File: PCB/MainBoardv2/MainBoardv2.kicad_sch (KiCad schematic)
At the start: 22 parts, among them J1 Conn_02x03_Odd_Even, SW1 SW_Push, U1 STM32F103C8T6TR

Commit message: Updating progress on board v2
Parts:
- added C11, C12: 20p, Capacitor_SMD:C_0603_1608Metric, symbol basic:C
- added C13: 10u, Capacitor_SMD:C_0603_1608Metric, symbol basic:C
- added C14: 22u, Capacitor_SMD:C_0805_2012Metric, symbol basic:C
- added J2: USB_B_Micro, symbol Connector:USB_B_Micro
- added J3: Conn_01x04_Pin, symbol Connector:Conn_01x04_Pin
- added J4, J7: Screw_Terminal_01x02, local:CONN_1985195, symbol Connector:Screw_Terminal_01x02
- added J5: Conn_02x03_Odd_Even, Connector_PinSocket_2.54mm:PinSocket_2x03_P2.54mm_Vertical, symbol Connector_Generic:Conn_02x03_Odd_Even
- added R4: 1k5, Resistor_SMD:R_0603_1608Metric, symbol basic:R
- added SW2: SW_SP3T, symbol Switch:SW_SP3T
- added U4: AZ1117-3.3, Package_TO_SOT_SMD:TO-252-2, symbol Regulator_Linear:AZ1117-3.3
- added Y1: 8MHz Crystal, Crystal:Crystal_HC49-U_Vertical, symbol Device:Crystal
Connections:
- net +3.3V: now also J3.1 (Pin_1), R4.1
- net GND: now also C11.1, C12.1, C13.2, C14.2, J2.5 (GND), J3.4 (Pin_4), J4.1 (Pin_1), J7.1 (Pin_1), U4.1 (GND)
- net TIM2_CH1: now reaches U1.10 (PA0)
- net TIM2_CH2: now reaches U1.11 (PA1)
- net SPI1_NSS_RasPi: now reaches U1.12 (PA2)
- net SPI1_NSS_ESP2: now reaches U1.13 (PA3)
- net SPI1_NSS_ESP1: now reaches U1.14 (PA4)
- net SPI1_SCK: now reaches U1.15 (PA5)
- net SPI1_MISO: now reaches U1.16 (PA6)
- net SPI1_MOSI: now reaches U1.17 (PA7)
- net TIM1_CH1: now reaches U1.29 (PA8)
- net TIM1_CH2: now reaches U1.30 (PA9)
- net TIM1_CH3: now reaches U1.31 (PA10)
- net USB_D-: now reaches U1.32 (PA11)
- net USB_D-: now also J2.2 (D-)
- net USB_D+: now reaches U1.33 (PA12)
- net USB_D+: now also J2.3 (D+), R4.2
- net SWDIO: now reaches U1.34 (PA13)
- net SWDIO: now also J3.2 (Pin_2)
- net SWCLK: now reaches U1.37 (PA14)
- net SWCLK: now also J3.3 (Pin_3)
- net TIM3_CH1: now reaches U1.40 (PB4)
- net TIM3_CH2: now reaches U1.41 (PB5)
- net TIM4_CH1: now reaches U1.42 (PB6)
- net TIM4_CH2: now reaches U1.43 (PB7)
- net OR3: now reaches U1.46 (PB9)
- net OSC_IN: now reaches U1.5 (PD0)
- net OSC_IN: now also C12.2, Y1.1
- net OSC_OUT: now reaches U1.6 (PD1)
- net OSC_OUT: now also C11.2, Y1.2
- new net +3V3: C14.1, J5.2 (Pin_2), J5.4 (Pin_4), U4.2 (VO)
- new net 12V_EXT: J4.2 (Pin_2)
- new net 5V_BUCK: SW2.2
- new net 5V_EXT: J5.5 (Pin_5), J7.2 (Pin_2), SW2.1
- new net REG_IN: C13.1, J5.3 (Pin_3), SW2.3, U4.3 (VI)
- new net VBUS: J2.1 (VBUS), J5.1 (Pin_1), SW2.4
- no-connect marks 22 -> 15
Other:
- added sheet LimitSwitchORGates (LimitSwitchOR.kicad_sch)
- note added: "+3.3V Power Mux"
- note added: "BOOT PINS"
- note added: "External Power Connectors"
- note added: "HIGH SPEED EXTERNAL (HSE) CRYSTAL OSCILLATOR - 8MHz"
- note added: "Limit Switch OR3"
- note added: "Linear Regulator"
- note added: "Microcontroller"
- note added: "RESET SWITCH"
- note added: "SERIAL WIRE DEBUG CONNECTOR"
- note added: "decide how we want handle this?"
- company: (none) -> University of Illinois Urbana-Champaign
- title: (none) -> ECE445_MainBoard
- moved on the sheet: C1, C10, C2, C3, C4, C5, C6, C7, C8, C9, FB1, J1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

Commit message: Update MainBoardv2.kicad_sch
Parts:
- removed J5: Conn_02x03_Odd_Even, Connector_PinSocket_2.54mm:PinSocket_2x03_P2.54mm_Vertical, symbol Connector_Generic:Conn_02x03_Odd_Even
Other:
- note added: "+3.3V Power Switch & Linear Regulator"
- note removed: "+3.3V Power Mux"
- note removed: "Linear Regulator"
- note removed: "decide how we want handle this?"
- moved on the sheet: C13, C14, SW2, U4

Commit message: updating main board v2 progress
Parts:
- removed C9: 4.7u, Capacitor_SMD:C_0603_1608Metric, symbol basic:C
- added C9: 100n, Capacitor_SMD:C_0603_1608Metric, symbol Device:C
- added Cboot, Cinx: 100nF, Capacitor_SMD:C_0805_2012Metric, symbol Device:C
- added Cff: 100pF, symbol Device:C
- added Cin: 15uF, Capacitor_SMD:C_0805_2012Metric, symbol Device:C
- added Cout: 47uF, Capacitor_SMD:C_1210_3225Metric, symbol Device:C
- added D1, D2, D4: LED, LED_THT:LED_D3.0mm_Clear, symbol Device:LED
- added J17, J18, J19: Conn_01x04_Socket, Connector_PinHeader_2.54mm:PinHeader_1x04_P2.54mm_Vertical, symbol Connector:Conn_01x04_Socket
- added J5: Conn_01x03_Socket, Connector_PinHeader_2.54mm:PinHeader_1x03_P2.54mm_Vertical, symbol Connector:Conn_01x03_Socket
- added L1: 3.3uH, CustomFootprints:IHLP3232DZER3R3M01, symbol Device:L
- added R5, R6, R7: 1.5k, Resistor_SMD:R_0603_1608Metric, symbol basic:R
- added Rfbb: 10k, Resistor_SMD:R_0805_2012Metric, symbol basic:R
- added Rfbt: 73.2k, Resistor_SMD:R_0805_2012Metric, symbol basic:R
- added Rff: 20k, Resistor_SMD:R_0603_1608Metric, symbol basic:R
- added Rpg: 100k, Resistor_SMD:R_0805_2012Metric, symbol basic:R
- added U5: TPS56637RPA, CustomFootprints:RPA0010A, symbol CustomSymbols:TPS56637RPA
- added U6: SN74HCS4075PWR, CustomFootprints:SN74HCS4075PWR, symbol CustomSymbols:SN74HCS4075PWR
- C8: value 100n -> 10u
- R4: value 1k5 -> 1.5k
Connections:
- net +3.3V: now also R5.1
- net 5V_BUCK: now also Cout.1, L1.2, Rfbt.2, Rff.2, Rpg.2
- net GND: now also C9.2, Cin.2, Cinx.2, Cout.2, D1.1 (K), D2.1 (K), D4.1 (K), Rfbb.1, U5.10 (MODE), U5.3 (AGND), U5.9 (PGND), U6.7 (GND)
- net OR3: now also U6.6 (1Y)
- net REG_IN: now also C9.1, R6.1, U6.1 (2A), U6.11 (3A), U6.12 (3B), U6.13 (3C), U6.14 (VCC), U6.2 (2B), U6.8 (2C)
- net SPI1_MISO: now also J17.2 (Pin_2), J18.2 (Pin_2), J19.2 (Pin_2)
- net SPI1_MOSI: now also J17.1 (Pin_1), J18.1 (Pin_1), J19.1 (Pin_1)
- net SPI1_NSS_ESP1: now also J17.4 (Pin_4)
- net SPI1_NSS_ESP2: now also J18.4 (Pin_4)
- net SPI1_NSS_RasPi: now also J19.4 (Pin_4)
- net SPI1_SCK: now also J17.3 (Pin_3), J18.3 (Pin_3), J19.3 (Pin_3)
- net 12V_EXT renamed +12V
- net +12V: now also Cin.1, Cinx.1, R7.1, U5.8 (VIN)
- new net: D1.2 (A), R5.2
- new net: Cff.1, Rff.1
- new net: D4.2 (A), R7.2
- new net: D2.2 (A), R6.2
- new net BOOT: Cboot.1, U5.7 (BOOT)
- new net FB: Cff.2, Rfbb.2, Rfbt.1, U5.2 (FB)
- new net LimitSwitch1: J5.1 (Pin_1), U6.5 (1C)
- new net LimitSwitch2: J5.2 (Pin_2), U6.4 (1B)
- new net LimitSwitch3: J5.3 (Pin_3), U6.3 (1A)
- new net PG: Rpg.1, U5.4 (PG)
- new net SW: Cboot.2, L1.1, U5.6 (SW)
- no-connect marks 15 -> 19
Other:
- removed sheet LimitSwitchORGates
- added sheet PWM & Encoders (PWM.kicad_sch)
- note added: "1x 100nF per VDD pin"
- note added: "4.5V to 28V, 6A Synchronous Buck Converter with ULQ-Mode Efficiency: 92.9% Frequency: 559.31kHz"
- note added: "6A Synchronous Buck Converter"
- note added: "Bypass cap. should be placed close to device"
- note added: "ESP32 (x2) & Raspberry Pi"
- note added: "LEDs"
- note added: "Microcontroller (and USB)"
- note added: "Pin-out using STM32CubeIDE"
- note added: "SPI BUS"
- note added: "USB Application Note: AN4879"
- note added: "Unused inputs should be tied to VCC"
- note added: "VBUS from USB Connector (nom. +5V) Min. 22uF inp./outp. caps"
- note added: "VDDA Filtering"
- note removed: "MOUNTING HOLES"
- note removed: "Microcontroller"
- moved on the sheet: C1, C11, C12, C2, C3, C4, C6, C8, H1, H2, H3, H4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

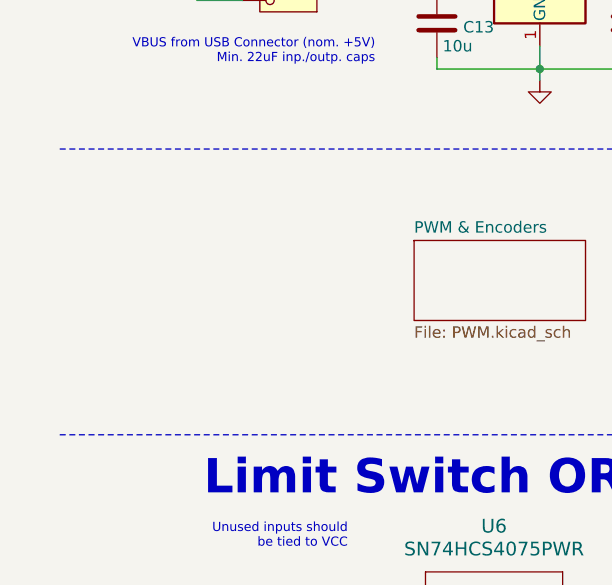
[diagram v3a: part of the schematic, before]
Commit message: updating main board v2 with motor power conns
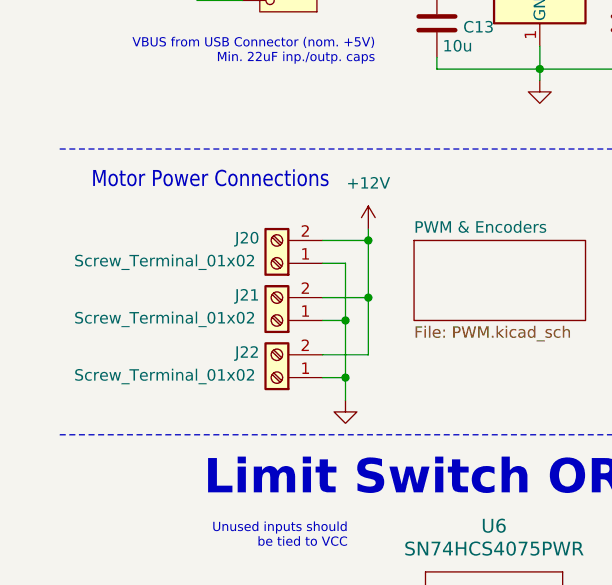
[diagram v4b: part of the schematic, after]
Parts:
- added J20, J21, J22: Screw_Terminal_01x02, local:CONN_1985195, symbol Connector:Screw_Terminal_01x02
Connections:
- net +12V: now also J20.2 (Pin_2), J21.2 (Pin_2), J22.2 (Pin_2)
- net GND: now also J20.1 (Pin_1), J21.1 (Pin_1), J22.1 (Pin_1)
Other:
- note added: "Motor Power Connections"

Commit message: updating progress for board v2
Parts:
- removed J20, J21, J22: Screw_Terminal_01x02, local:CONN_1985195, symbol Connector:Screw_Terminal_01x02
- removed J3: Conn_01x04_Pin, symbol Connector:Conn_01x04_Pin
- added J23: Conn_01x05_Pin, symbol Connector:Conn_01x05_Pin
- added SW4: ~, CustomFootprints:MTM8206NRA, symbol CustomSymbols:SW_Toggle_DPDT
- added TP10, TP7, TP8, TP9: ~, TestPoint:TestPoint_Keystone_5000-5004_Miniature, symbol Connector:TestPoint
- added TP2: 5V, TestPoint:TestPoint_Keystone_5000-5004_Miniature, symbol Connector:TestPoint
- added TP3: 12V, TestPoint:TestPoint_Keystone_5000-5004_Miniature, symbol Connector:TestPoint
- Cff: footprint (none) -> Capacitor_SMD:C_0805_2012Metric
- FB1: footprint (none) -> Inductor_SMD:L_0603_1608Metric
- Rff: footprint Resistor_SMD:R_0603_1608Metric -> Resistor_SMD:R_0805_2012Metric
- TP1: value 3V3 -> 3.3V
- renumbered C5 to C1, C14 to C10, C1 to C11, C11 to C12, C9 to C13, C12 to C14, C7 to C2, C10 to C3, C2 to C4, C3 to C5, C4 to C6, C6 to C7, C13 to C9, Cout to Cout1, D4 to D3, J19 to J10, J17 to J11, J18 to J12, J1 to J4, J5 to J7, J4 to J8, J7 to J9, R5 to R1, R6 to R2, R7 to R3, R1 to R5, R2 to R6, R3 to R7, SW2 to SW1, SW1 to SW2, U4 to U1, U1 to U2, U6 to U3, U5 to U4
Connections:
- net +3V3 is gone; now on net +3.3V: C10.1, U1.2 (VO)
- net +12V: now also D3.2 (A), SW4.2 (B), SW4.5 (B), TP3.1; no longer J8.2 (Pin_2), R3.1
- net +3.3V: now also D1.2 (A), J23.1 (Pin_1); no longer R1.1
- net GND: now also R1.2, R2.2, R3.2, J23.5 (Pin_5); no longer D1.1 (K), D2.1 (K), D3.1 (K)
- net NRST: now also J23.4 (Pin_4)
- net OR3: now also TP7.1
- net REG_IN: now also D2.2 (A), TP2.1; no longer R2.1
- net SPI1_MISO: now also TP9.1
- net SPI1_MOSI: now also TP10.1
- net SPI1_SCK: now also TP8.1
- net SWCLK: now also J23.3 (Pin_3)
- net SWDIO: now also J23.2 (Pin_2)
- net Cff_Rff: now reaches Cff.1, Rff.1
- new net: J8.2 (Pin_2), SW4.1 (A), SW4.4 (A)
- new net PWR_LED_12V_Cathode: D3.1 (K), R3.1
- new net PWR_LED_3V3_Cathode: D1.1 (K), R1.1
- new net PWR_LED_5V_Cathode: D2.1 (K), R2.1
- no-connect marks 19 -> 21
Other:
- added sheet Motors (Motors.kicad_sch)
- note added: "6A Buck chosen to leave headroom for a future iteration where 5V external devices are powered through this board"
- note removed: "Motor Power Connections"
- moved on the sheet: C11, C12, C14, D1, D2, D3, J10, J11, J12, J8, J9, R1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

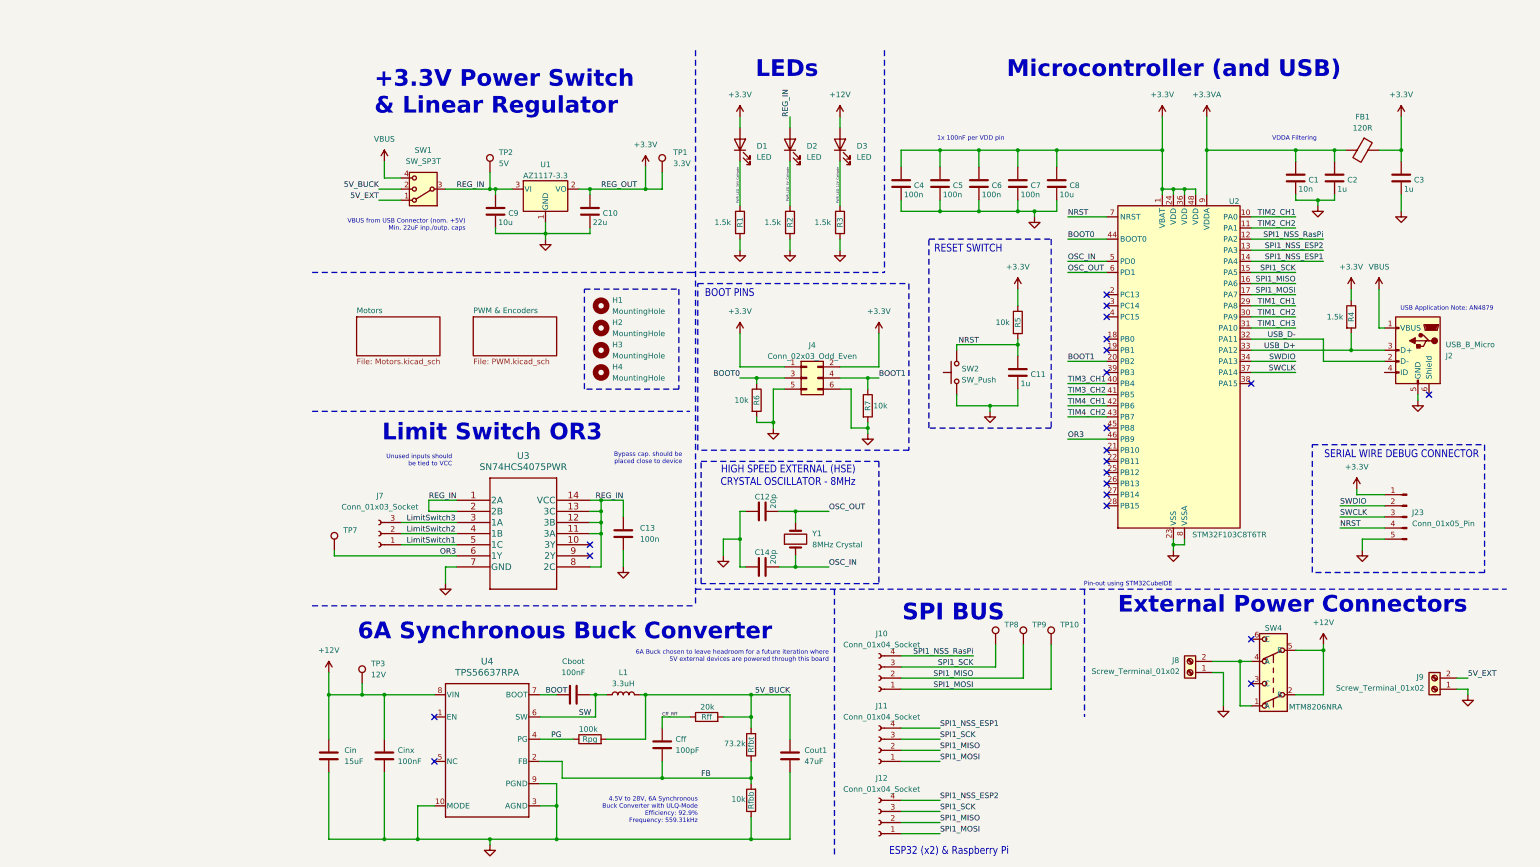
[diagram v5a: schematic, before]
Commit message: board v2 passing ERC in schematic
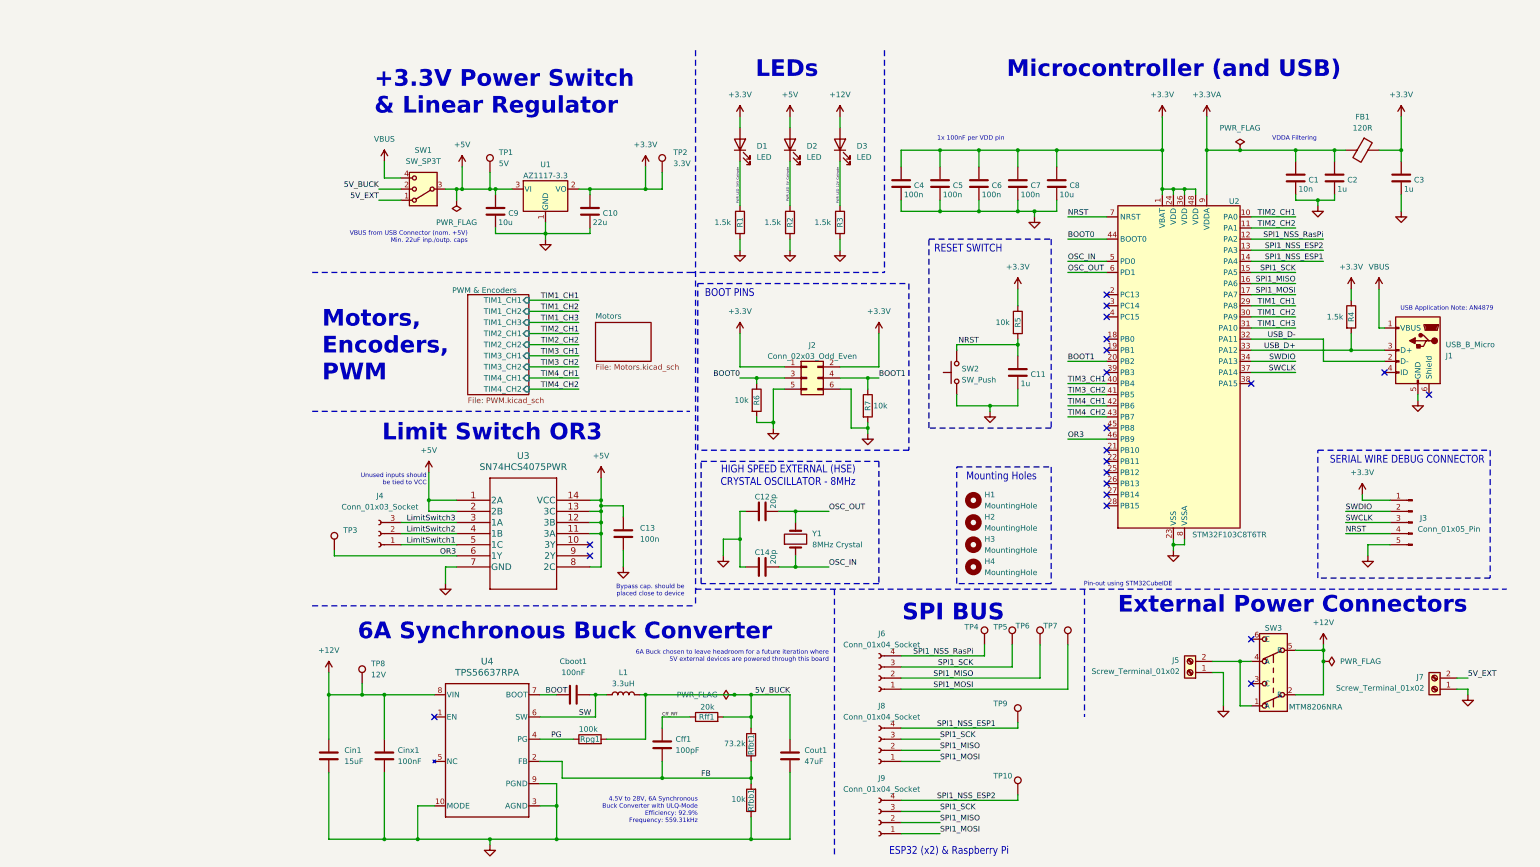
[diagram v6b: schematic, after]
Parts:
- added TP10, TP7, TP9: ~, TestPoint:TestPoint_Keystone_5000-5004_Miniature, symbol Connector:TestPoint
- U4: footprint CustomFootprints:RPA0010A -> RPA0010A
- renumbered Cboot to Cboot1, Cff to Cff1, Cin to Cin1, Cinx to Cinx1, J2 to J1, J4 to J2, J23 to J3, J7 to J4, J8 to J5, J10 to J6, J9 to J7, J11 to J8, J12 to J9, Rfbb to Rfbb1, Rfbt to Rfbt1, Rff to Rff1, Rpg to Rpg1, SW4 to SW3, TP2 to TP1, TP1 to TP2, TP7 to TP3, TP8 to TP4, TP9 to TP5, TP10 to TP6, TP3 to TP8
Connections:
- net SPI1_MISO: now also TP6.1; no longer TP5.1
- net SPI1_MOSI: now also TP7.1; no longer TP6.1
- net SPI1_NSS_ESP1: now also TP9.1
- net SPI1_NSS_ESP2: now also TP10.1
- net SPI1_NSS_RasPi: now also TP4.1
- net SPI1_SCK: now also TP5.1; no longer TP4.1
- net REG_IN renamed +5V
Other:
- sheet PWM & Encoders ports: added TIM1_CH1, TIM1_CH2, TIM1_CH3, TIM2_CH1, TIM2_CH2, TIM3_CH1, TIM3_CH2, TIM4_CH1, TIM4_CH2; removed none
- note added: "Motors, Encoders, PWM"
- note added: "Mounting Holes"
- moved on the sheet: H1, H2, H3, H4, J3, TP4, TP5, TP6

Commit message: footprints all assigned for board v2
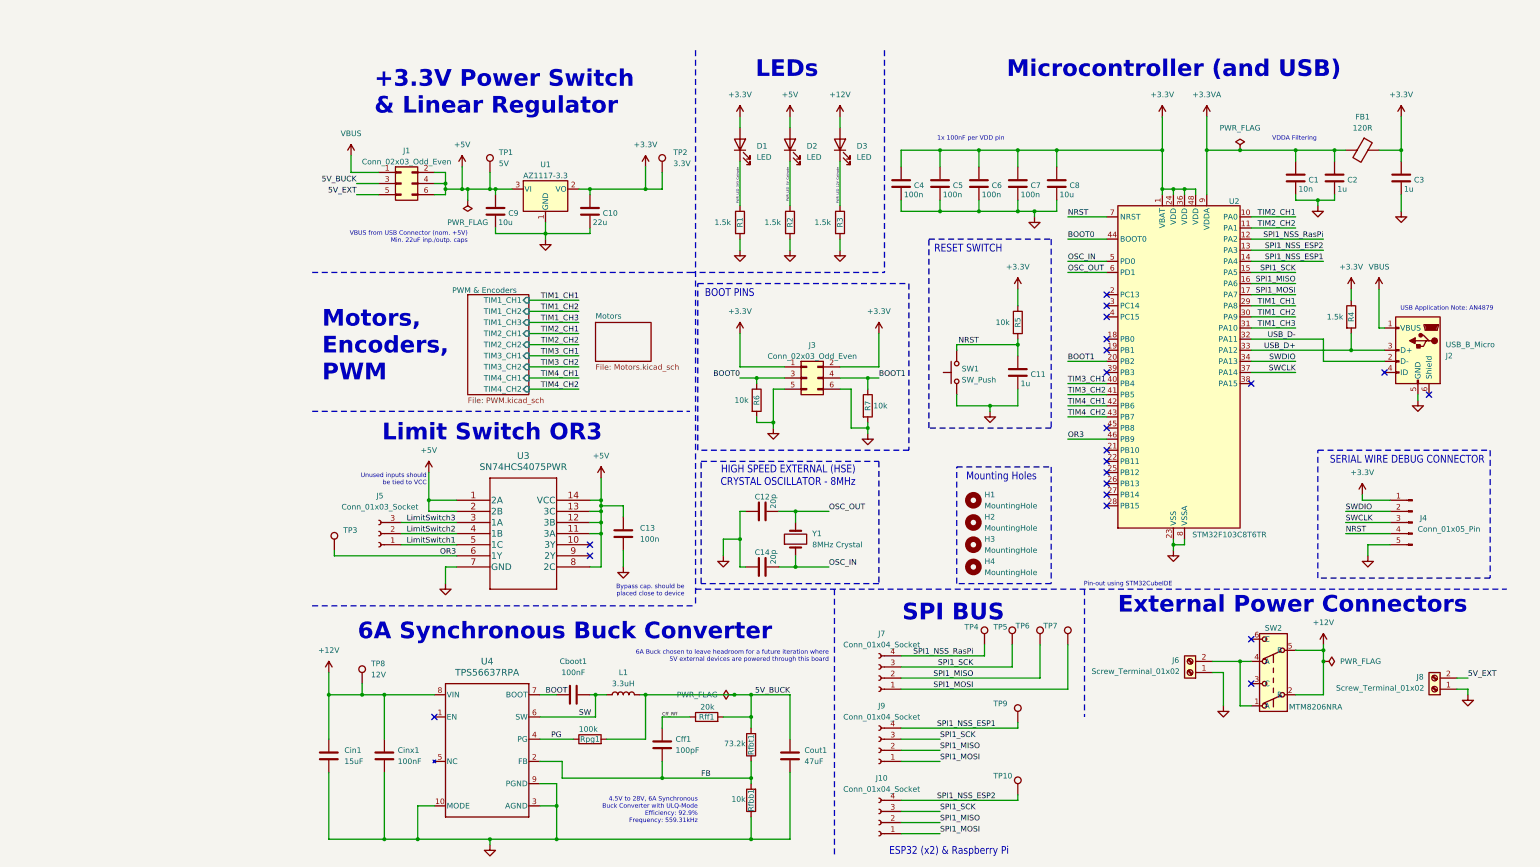
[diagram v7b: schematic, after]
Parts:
- removed SW1: SW_SP3T, symbol Switch:SW_SP3T
- added J1: Conn_02x03_Odd_Even, Connector_PinSocket_2.54mm:PinSocket_2x03_P2.54mm_Vertical, symbol Connector_Generic:Conn_02x03_Odd_Even
- D1, D2, D3: footprint LED_THT:LED_D3.0mm_Clear -> LED_SMD:LED_0603_1608Metric
- J2: renamed from J1; footprint (none) -> CustomFootprints:AMPHENOL_10118192-0002LF
- J4: renamed from J3; footprint (none) -> Connector_PinSocket_2.54mm:PinSocket_1x05_P2.54mm_Vertical
- J6: renamed from J5; footprint local:CONN_1985195 -> CustomFootprints:1985195
- J8: renamed from J7; footprint local:CONN_1985195 -> CustomFootprints:1985195
- U4: footprint RPA0010A -> CustomFootprints:RPA0010A
- renumbered J9 to J10, J2 to J3, J4 to J5, J6 to J7, J8 to J9, SW2 to SW1, SW3 to SW2
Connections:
- net +5V: now also J1.2 (Pin_2), J1.4 (Pin_4), J1.6 (Pin_6)
- net 5V_BUCK: now also J1.3 (Pin_3)
- net 5V_EXT: now also J1.5 (Pin_5)
- net VBUS: now also J1.1 (Pin_1)
